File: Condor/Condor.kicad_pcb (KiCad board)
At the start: 2 copper layers, 40 x 40 mm, 6 parts

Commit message: updated condor board
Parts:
- added REF**: diode_direction, Symbol:diode_direction, F.Cu at (179.8, 100.2)
- 10 nF: renamed from REF**
- 50 Ω: renamed from REF**; value R_0603_1608Metric -> R_1206_3216Metric; footprint Resistor_SMD:R_0603_1608Metric -> Resistor_SMD:R_1206_3216Metric
- moved REF** 2.24 mm to (175.0, 91.8)
- moved 50 Ω 1.50 mm to (168.0, 101.5)
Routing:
- net (no net): track 92.5 -> 95.8 mm
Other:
- board text added: "Designed by Sebouh Paul UC Riverside Version v2"
- board text added: "GND"
- board text added: "SiPM HV"
- board text added: "SiPM Sig"
- board text added: "Temp Sig"
- board text added: "Temp VDD"

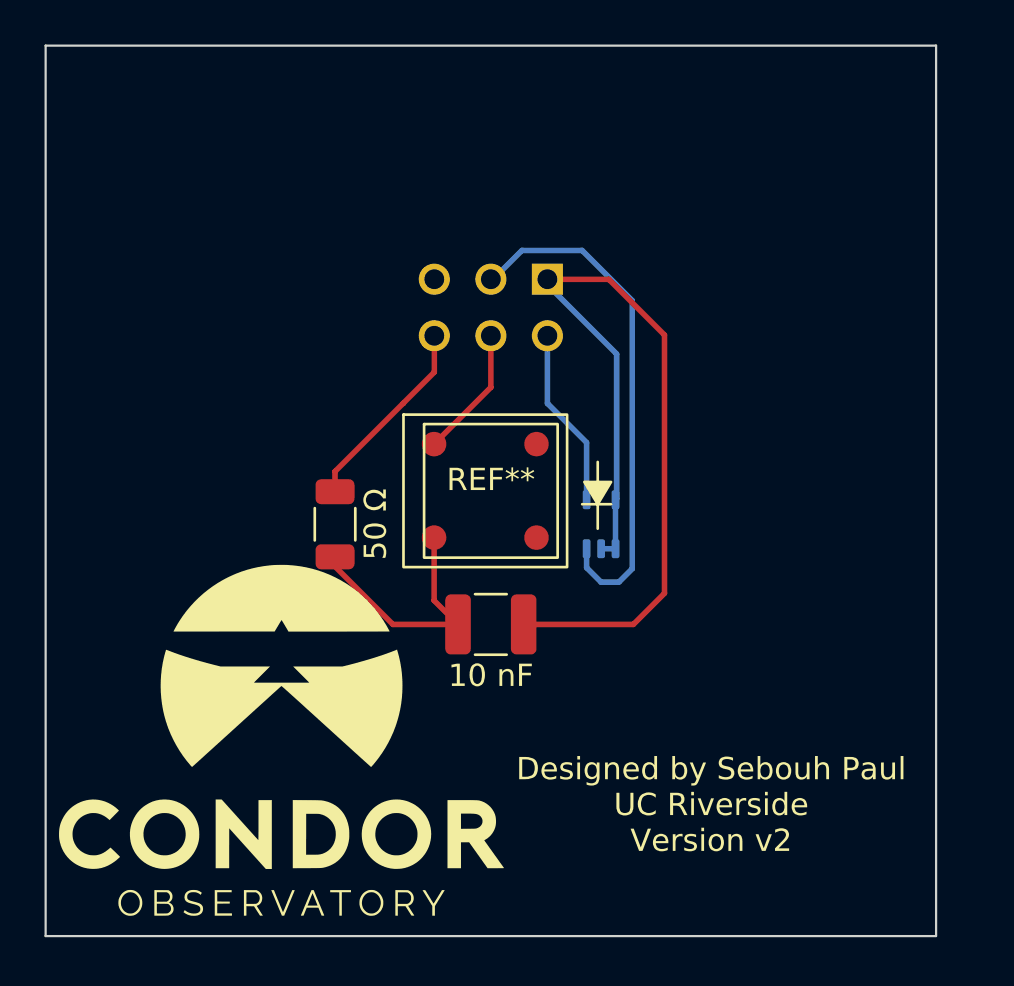
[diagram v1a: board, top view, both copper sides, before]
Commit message: updated condor board (v3, with 2 6-pin connectors, matching the uDAQ
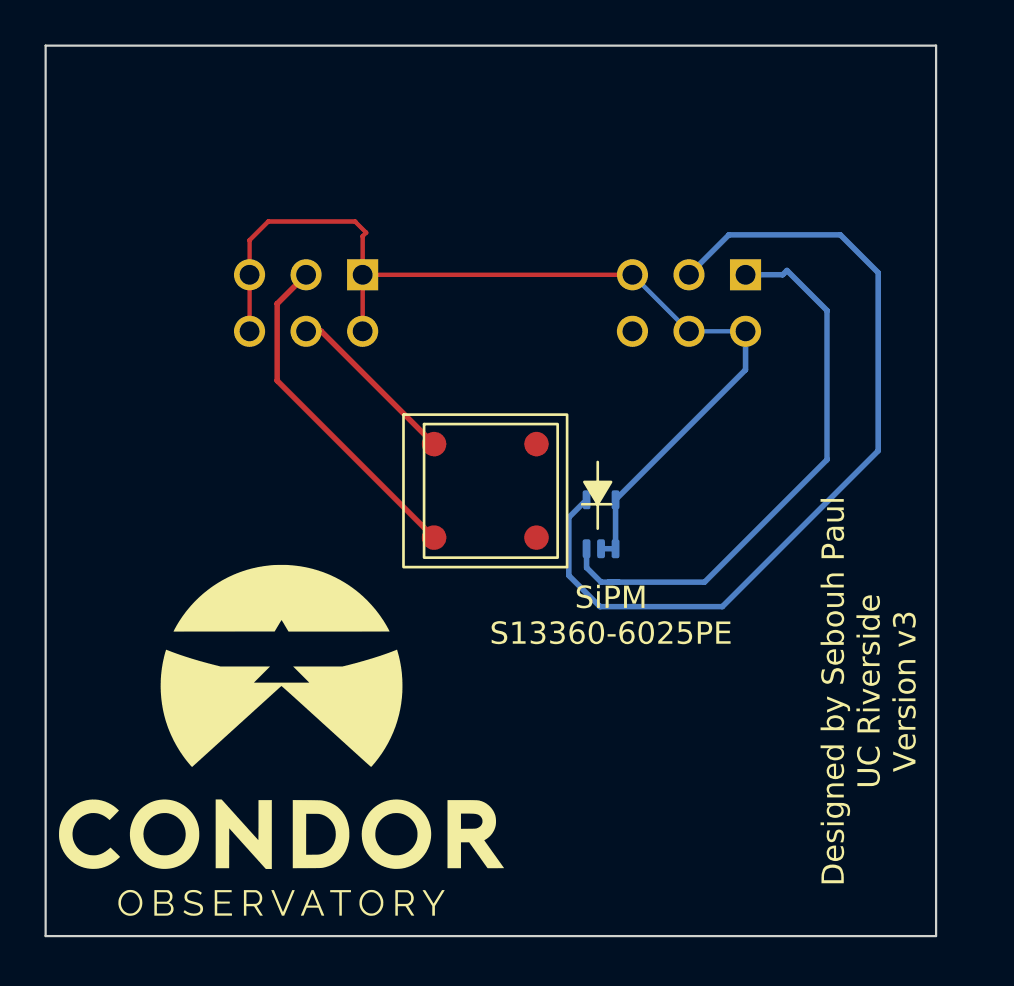
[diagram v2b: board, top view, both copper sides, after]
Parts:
- removed 10 nF: C_1210_3225Metric, Capacitor_SMD:C_1210_3225Metric
- removed 50 Ω: R_1206_3216Metric, Resistor_SMD:R_1206_3216Metric
- added REF**: TE_2-1761679-1, Connector_TE-Connectivity:TE_2-1761679-1, B.Cu at (183.9, 91.6)
- moved REF** 8.30 mm to (166.7, 91.6)
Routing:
- net (no net): track 95.8 -> 133.5 mm
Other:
- board text added: "ANODE"
- board text added: "CATHODE"
- board text added: "Connector for SiPM"
- board text added: "Connector for Temp"
- board text added: "Designed by Sebouh Paul UC Riverside Version v3"
- board text added: "OUT"
- board text added: "SiPM S13360-6025PE"
- board text added: "Temp Sensor LM94021QBIMG/NOPB"
- board text added: "Unused"
- board text added: "VDD"
- board text removed: "Designed by Sebouh Paul UC Riverside Version v2"
- board text removed: "SiPM HV"
- board text removed: "SiPM Sig"
- board text removed: "Temp Sig"
- board text removed: "Temp VDD"

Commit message: updated condor board (v4, with 2 6-pin connectors on left and right of center, matching the physical positions of the uDAQ pins)
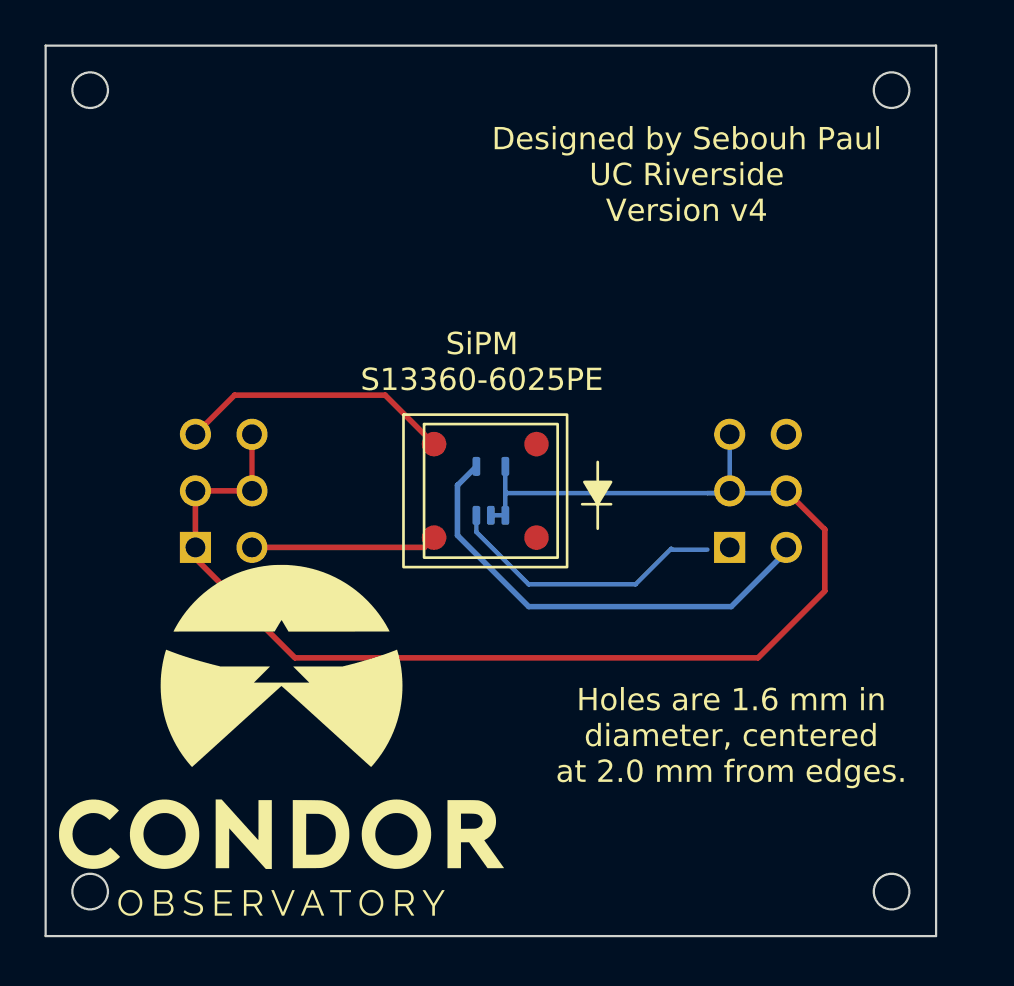
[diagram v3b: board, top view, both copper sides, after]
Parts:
- moved REF** 9.21 mm to (163.0, 100.0), turned to 90 degrees
- moved REF** 8.99 mm to (187.0, 100.0), turned to 90 degrees
- moved REF** 5.17 mm to (175.0, 100.0)
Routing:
- net (no net): track 133.5 -> 118.0 mm
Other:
- outline, holes or cut-outs redrawn
- board text added: "Designed by Sebouh Paul UC Riverside Version v4"
- board text added: "Holes are 1.6 mm in diameter, centered at 2.0 mm from edges."
- board text removed: "Connector for Temp"
- board text removed: "Designed by Sebouh Paul UC Riverside Version v3"
- board text removed: "Unused"

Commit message: updated condor board; added an additional label
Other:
- board text added: "Connector for temp sensor"
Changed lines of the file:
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@@
+    (effects (font (size 1 1) (thickness 0.15)) (justify mirror))
+  )
+  (gr_text "Connector for \ntemp sensor" (at 187.5 90.2) (layer "B.SilkS")
     (effects (font (size 1 1) (thickness 0.15)) (justify mirror))
   )
